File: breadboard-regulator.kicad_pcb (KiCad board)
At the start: 2 copper layers, 16 parts, among them J1 Barrel_Jack_Switch, U1 LM7805_TO220, U2 LD1117S33TR_SOT223

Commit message: finish schematic and PCB design
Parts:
- added J2: Conn_01x02_Pin, Connector_PinHeader_2.54mm:PinHeader_1x02_P2.54mm_Vertical, F.Cu at (224.7, 87.5)
- added J3: Conn_01x02_Pin, Connector_PinHeader_2.54mm:PinHeader_1x02_P2.54mm_Vertical, F.Cu at (224.3, 121.9)
- U2: value LD1117S33TR_SOT223 -> LD1117V33_TO-220
- moved D2 15.9 mm to (214.1, 90.7), turned to 180 degrees
- moved D3 15.8 mm to (213.7, 126.0), turned to 180 degrees
- moved CNF4 5.46 mm to (183.1, 126.2)
- moved CNF3 4.40 mm to (130.2, 124.5)
- moved CNF2 4.22 mm to (183.1, 90.7)
- moved J1 3.76 mm to (83.1, 113.3)
- moved R1 3.22 mm to (203.1, 90.7)
- moved U1 2.80 mm to (148.4, 90.8)
- moved R2 1.78 mm to (204.6, 126.2)
- moved C2 1.03 mm to (171.0, 90.8)
- moved C1 0.41 mm to (113.7, 90.6)
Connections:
- D2 pad 1: unconnected-(D2-K-Pad1) -> GND
- D3 pad 1: unconnected-(D3-K-Pad1) -> GND
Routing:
- net GND: track 0.00 -> 391.8 mm
- net Net-(D1-K): track 0.00 -> 137.1 mm
- net +3.3V: track 0.00 -> 92.9 mm
- net +5V: track 0.00 -> 76.6 mm
- net Net-(D2-A): track 0.00 -> 8.52 mm
- net Net-(D1-A): track 0.00 -> 6.89 mm
- net Net-(D3-A): track 0.00 -> 6.66 mm
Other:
- board outline added: 166.1 x 51.2 mm
- board text added: "+3.3V"
- board text added: "+5V"
- board text added: "GND"
- board text added: "VCC"

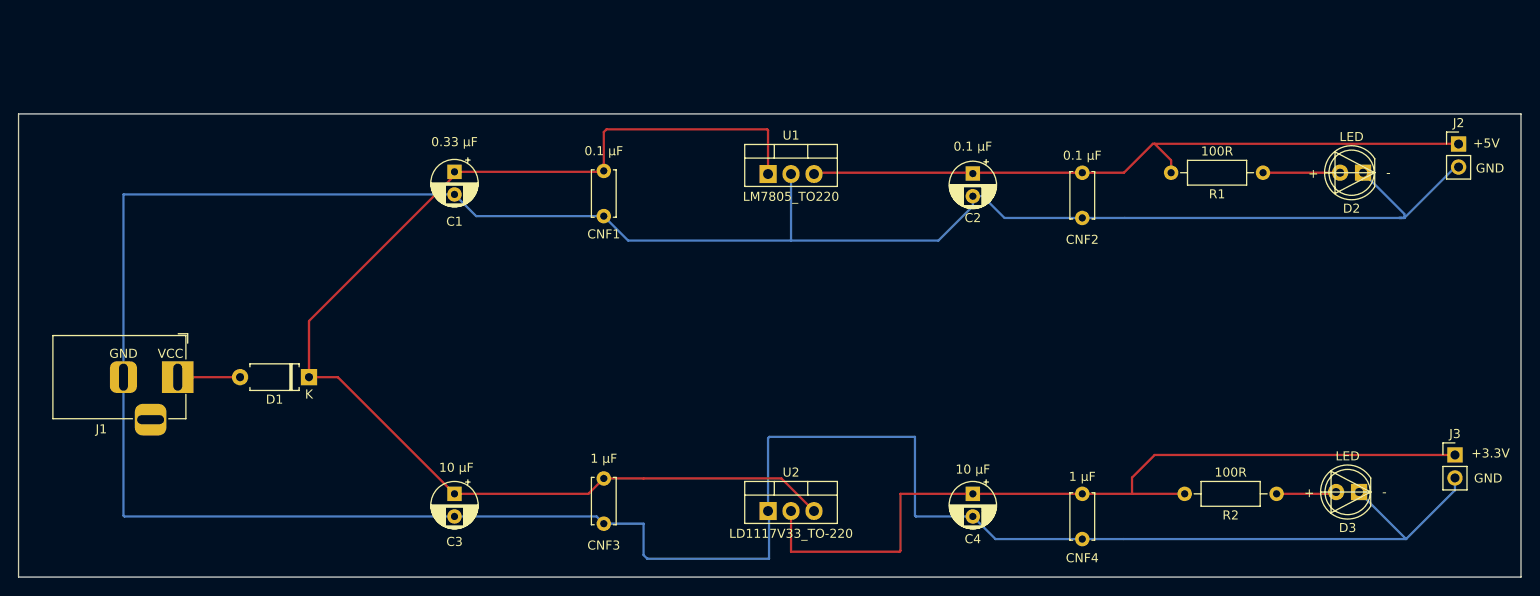
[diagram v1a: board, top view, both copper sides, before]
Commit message: split schematics diagram; rearrange PCB
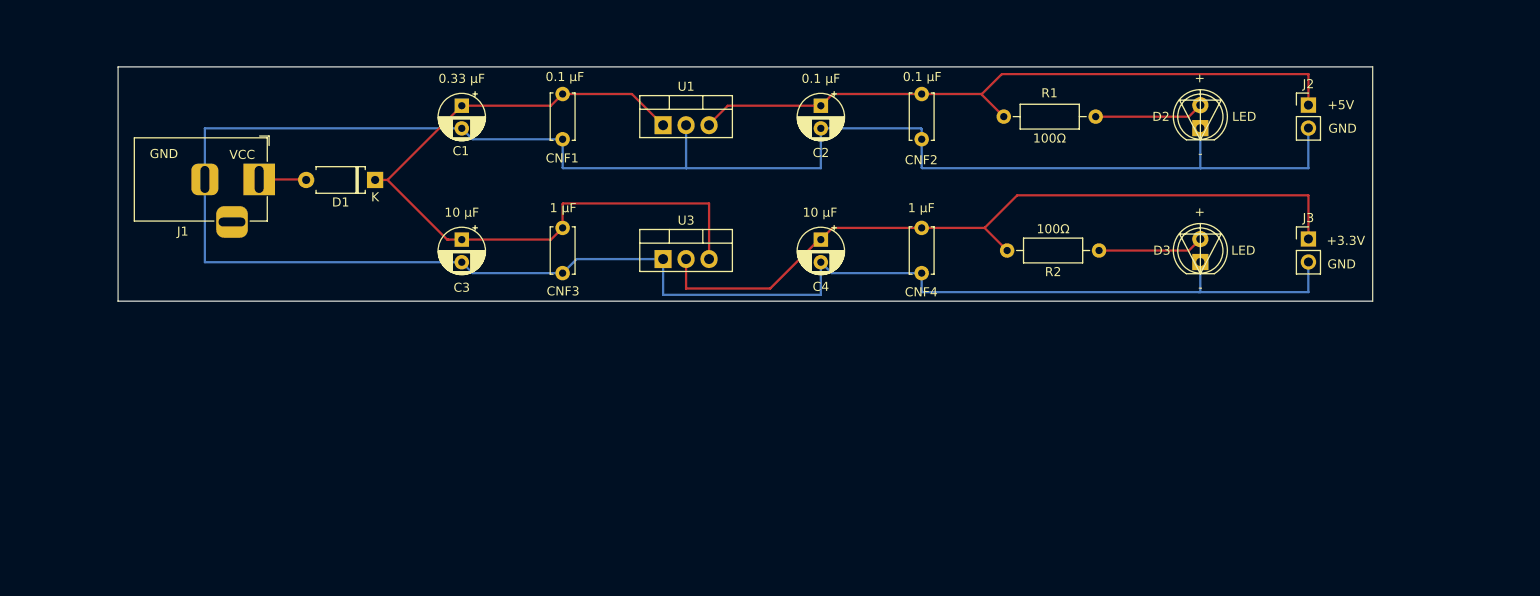
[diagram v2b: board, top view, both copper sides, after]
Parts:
- removed U2: LD1117V33_TO-220, Package_TO_SOT_THT:TO-220-3_Vertical
- added U3: LD1117V33_TO-220, Package_TO_SOT_THT:TO-220-3_Vertical, F.Cu at (136.8, 100.2)
- R1, R2: value 100R -> 100Ω
- moved CNF4 34.3 mm to (165.3, 96.8)
- moved R2 33.3 mm to (185.0, 99.3)
- moved C4 32.7 mm to (154.2, 98.1)
- moved D3 30.9 mm to (196.2, 100.6), turned to 90 degrees
- moved J3 28.9 mm to (208.1, 98.0)
- moved C3 28.1 mm to (114.5, 98.1)
- moved CNF3 28.1 mm to (125.6, 96.8)
- moved J1 23.6 mm to (92.1, 91.4)
- moved D1 23.0 mm to (104.9, 91.5)
- moved CNF2 19.8 mm to (165.3, 82.0)
- moved R1 19.5 mm to (184.6, 84.5)
- moved D2 18.7 mm to (196.2, 85.8), turned to 90 degrees
- moved C2 18.4 mm to (154.2, 83.3)
- moved J2 17.1 mm to (208.1, 83.2)
- moved U1 12.8 mm to (136.8, 85.4)
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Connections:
- net Net-(D1-K) renamed +12V
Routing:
- net GND: track 391.8 -> 302.9 mm
- net +12V: track 137.1 -> 84.8 mm
- net +3.3V: track 92.9 -> 84.7 mm
- net Net-(D3-A): track 6.66 -> 11.7 mm
- net Net-(D2-A): track 8.52 -> 12.1 mm
- net Net-(D1-A): track 6.89 -> 5.22 mm
- net +5V: track 76.6 -> 75.6 mm
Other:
- board size 166.1 x 51.2 mm -> 138.7 x 25.9 mm

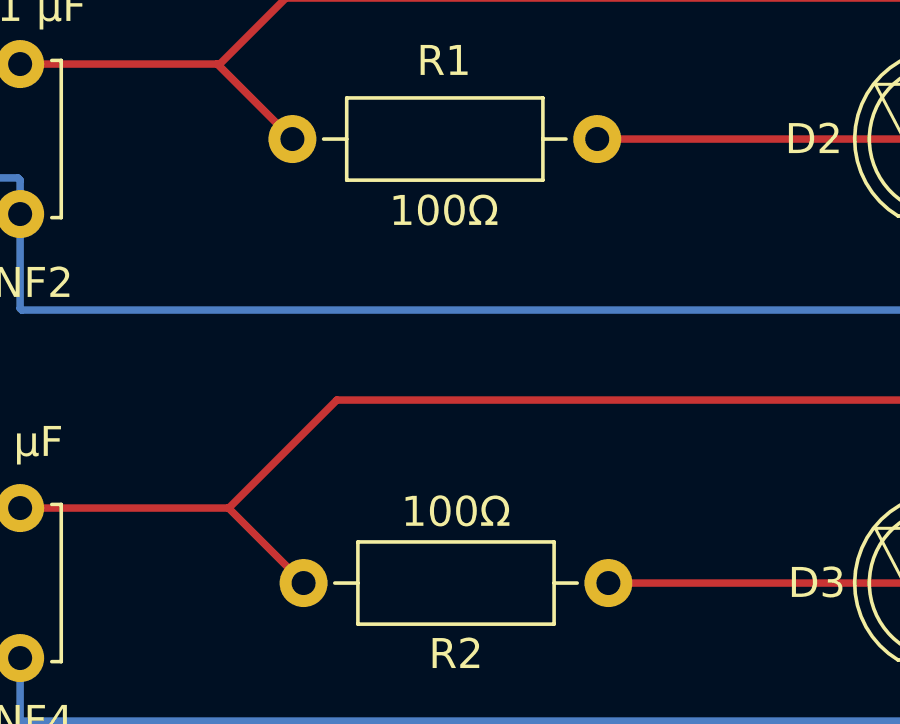
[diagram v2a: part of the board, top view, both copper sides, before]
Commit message: modify net number
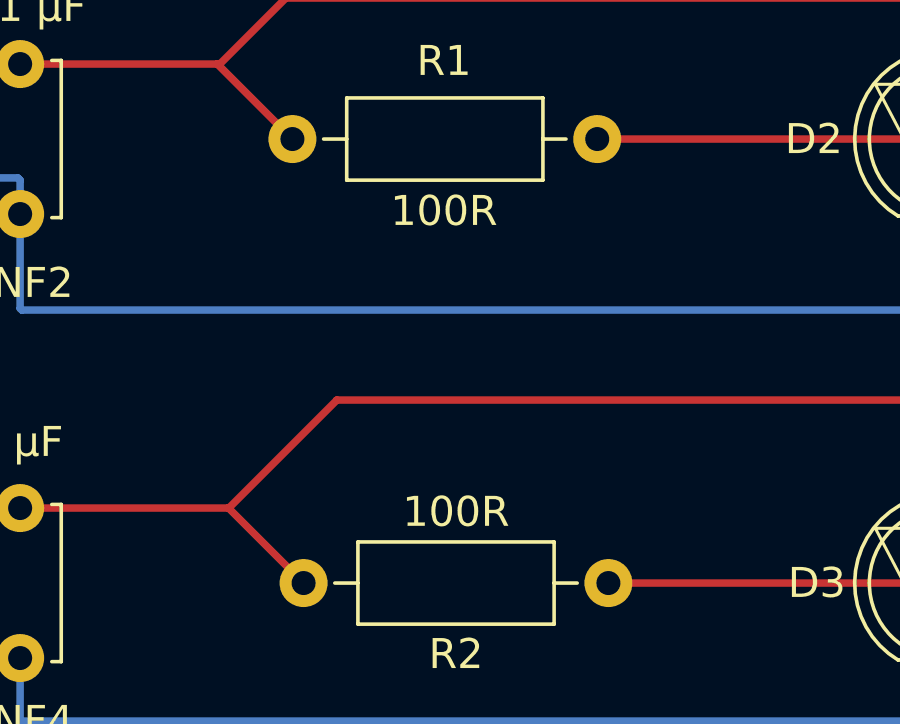
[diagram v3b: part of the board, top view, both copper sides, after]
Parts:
- R1, R2: value 100Ω -> 100R
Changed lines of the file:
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@@
   (net 3 "+5V")
   (net 4 "+3.3V")
-  (net 5 "Net-(D1-A)")
-  (net 6 "Net-(D2-A)")
-  (net 7 "Net-(D3-A)")
-  (net 8 "unconnected-(J1-Pad3)")
+  (net 5 "Net-(D2-A)")
+  (net 6 "Net-(D3-A)")
+  (net 7 "unconnected-(J1-Pad3)")
+  (net 8 "Net-(D1-A)")
   (footprint "Connector_BarrelJack:BarrelJack_Horizontal" (layer "F.Cu")
     (at 92.1 91.4425)
@@
       (stroke (width 0.1) (type solid)) (layer "F.Fab"))
     (pad "1" thru_hole rect (at 0 0) (size 3.5 3.5) (drill oval 1 3) (layers "*.Cu" "*.Mask")
-      (net 5 "Net-(D1-A)") (pintype "passive"))
+      (net 8 "Net-(D1-A)") (pintype "passive"))
     (pad "2" thru_hole roundrect (at -6 0) (size 3 3.5) (drill oval 1 3) (layers "*.Cu" "*.Mask") (roundrect_rratio 0.25)
       (net 2 "GND") (pintype "passive"))
     (pad "3" thru_hole roundrect (at -3 4.7) (size 3.5 3.5) (drill oval 3 1) (layers "*.Cu" "*.Mask") (roundrect_rratio 0.25)
-      (net 8 "unconnected-(J1-Pad3)") (pintype "passive+no_connect"))
+      (net 7 "unconnected-(J1-Pad3)") (pintype "passive+no_connect"))
     (model "${KICAD6_3DMODEL_DIR}/Connector_BarrelJack.3dshapes/BarrelJack_Horizontal.wrl"
       (offset (xyz 0 0 0))
@@
         (effects (font (size 1 1) (thickness 0.15)))
     )
-    (fp_text value "100Ω" (at 5.08 2.37) (layer "F.SilkS")
+    (fp_text value "100R" (at 5.08 2.37) (layer "F.SilkS")
         (effects (font (size 1 1) (thickness 0.15)))
     )
@@
       (stroke (width 0.1) (type solid)) (layer "F.Fab"))
     (pad "1" thru_hole circle (at 0 0 180) (size 1.6 1.6) (drill 0.8) (layers "*.Cu" "*.Mask")
-      (net 7 "Net-(D3-A)") (pintype "passive"))
+      (net 6 "Net-(D3-A)") (pintype "passive"))
     (pad "2" thru_hole oval (at 10.16 0 180) (size 1.6 1.6) (drill 0.8) (layers "*.Cu" "*.Mask")
       (net 4 "+3.3V") (pintype "passive"))
@@
       (net 2 "GND") (pinfunction "K") (pintype "passive"))
     (pad "2" thru_hole circle (at 2.54 0 90) (size 1.8 1.8) (drill 0.9) (layers "*.Cu" "*.Mask")
-      (net 6 "Net-(D2-A)") (pinfunction "A") (pintype "passive"))
+      (net 5 "Net-(D2-A)") (pinfunction "A") (pintype "passive"))
     (model "${KICAD6_3DMODEL_DIR}/LED_THT.3dshapes/LED_D5.0mm.wrl"
       (offset (xyz 0 0 0))
@@
       (net 1 "+12V") (pinfunction "K") (pintype "passive"))
     (pad "2" thru_hole oval (at 7.62 0 180) (size 1.8 1.8) (drill 0.9) (layers "*.Cu" "*.Mask")
-      (net 5 "Net-(D1-A)") (pinfunction "A") (pintype "passive"))
+      (net 8 "Net-(D1-A)") (pinfunction "A") (pintype "passive"))
     (model "${KICAD6_3DMODEL_DIR}/Diode_THT.3dshapes/D_A-405_P7.62mm_Horizontal.wrl"
       (offset (xyz 0 0 0))
@@
       (net 2 "GND") (pinfunction "K") (pintype "passive"))
     (pad "2" thru_hole circle (at 2.54 0 90) (size 1.8 1.8) (drill 0.9) (layers "*.Cu" "*.Mask")
-      (net 7 "Net-(D3-A)") (pinfunction "A") (pintype "passive"))
+      (net 6 "Net-(D3-A)") (pinfunction "A") (pintype "passive"))
     (model "${KICAD6_3DMODEL_DIR}/LED_THT.3dshapes/LED_D5.0mm.wrl"
       (offset (xyz 0 0 0))
@@
         (effects (font (size 1 1) (thickness 0.15)))
     )
-    (fp_text value "100Ω" (at 5.107145 -2.4) (layer "F.SilkS")
+    (fp_text value "100R" (at 5.107145 -2.4) (layer "F.SilkS")
         (effects (font (size 1 1) (thickness 0.15)))
     )
@@
       (stroke (width 0.1) (type solid)) (layer "F.Fab"))
     (pad "1" thru_hole circle (at 0 0 180) (size 1.6 1.6) (drill 0.8) (layers "*.Cu" "*.Mask")
-      (net 6 "Net-(D2-A)") (pintype "passive"))
+      (net 5 "Net-(D2-A)") (pintype "passive"))
     (pad "2" thru_hole oval (at 10.16 0 180) (size 1.6 1.6) (drill 0.8) (layers "*.Cu" "*.Mask")
       (net 3 "+5V") (pintype "passive"))
@@
   (segment (start 172.292855 96.8) (end 174.792855 99.3) (width 0.25) (layer "F.Cu") (net 4))
   (segment (start 154.005112 98.094888) (end 154.195713 98.094888) (width 0.25) (layer "F.Cu") (net 4))
-  (segment (start 97.2425 91.4425) (end 97.3 91.5) (width 0.25) (layer "F.Cu") (net 5))
-  (segment (start 92.1 91.4425) (end 97.2425 91.4425) (width 0.25) (layer "F.Cu") (net 5))
-  (segment (start 184.58 84.5) (end 194.886426 84.5) (width 0.25) (layer "F.Cu") (net 6))
-  (segment (start 194.886426 84.5) (end 196.151426 83.235) (width 0.25) (layer "F.Cu") (net 6))
-  (segment (start 184.952855 99.3) (end 194.886426 99.3) (width 0.25) (layer "F.Cu") (net 7))
-  (segment (start 194.886426 99.3) (end 196.151426 98.035) (width 0.25) (layer "F.Cu") (net 7))
+  (segment (start 184.58 84.5) (end 194.886426 84.5) (width 0.25) (layer "F.Cu") (net 5))
+  (segment (start 194.886426 84.5) (end 196.151426 83.235) (width 0.25) (layer "F.Cu") (net 5))
+  (segment (start 184.952855 99.3) (end 194.886426 99.3) (width 0.25) (layer "F.Cu") (net 6))
+  (segment (start 194.886426 99.3) (end 196.151426 98.035) (width 0.25) (layer "F.Cu") (net 6))
+  (segment (start 97.2425 91.4425) (end 97.3 91.5) (width 0.25) (layer "F.Cu") (net 8))
+  (segment (start 92.1 91.4425) (end 97.2425 91.4425) (width 0.25) (layer "F.Cu") (net 8))
 )

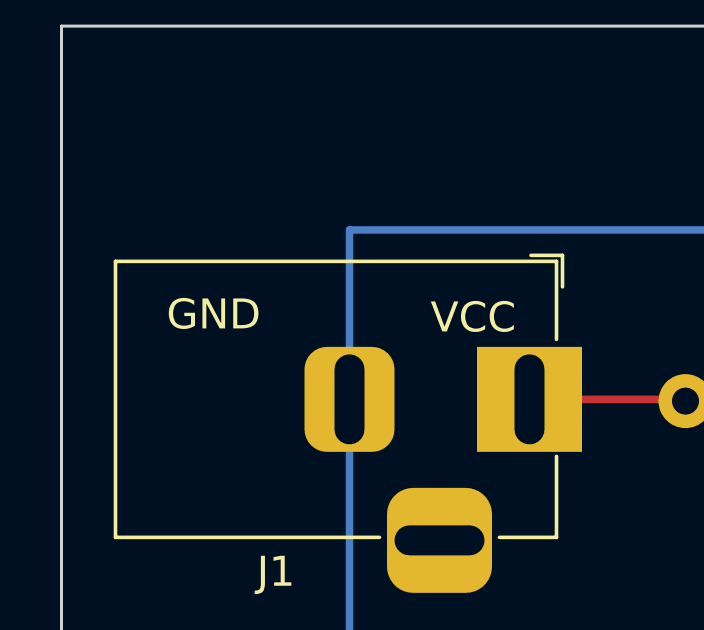
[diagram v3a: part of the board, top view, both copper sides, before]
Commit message: change from GND to GNDREF
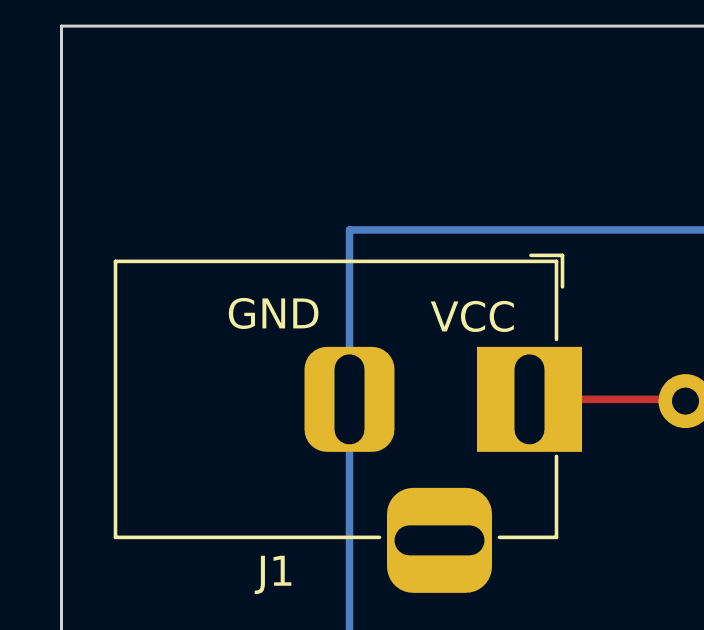
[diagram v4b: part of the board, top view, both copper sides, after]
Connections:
- net GND renamed GNDREF
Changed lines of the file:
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@@
   (net 0 "")
   (net 1 "+12V")
-  (net 2 "GND")
+  (net 2 "GNDREF")
   (net 3 "+5V")
   (net 4 "+3.3V")
@@
       (net 8 "Net-(D1-A)") (pintype "passive"))
     (pad "2" thru_hole roundrect (at -6 0) (size 3 3.5) (drill oval 1 3) (layers "*.Cu" "*.Mask") (roundrect_rratio 0.25)
-      (net 2 "GND") (pintype "passive"))
+      (net 2 "GNDREF") (pintype "passive"))
     (pad "3" thru_hole roundrect (at -3 4.7) (size 3.5 3.5) (drill oval 3 1) (layers "*.Cu" "*.Mask") (roundrect_rratio 0.25)
       (net 7 "unconnected-(J1-Pad3)") (pintype "passive+no_connect"))
@@
       (net 3 "+5V") (pinfunction "Pin_1") (pintype "passive"))
     (pad "2" thru_hole oval (at 0 2.54) (size 1.7 1.7) (drill 1) (layers "*.Cu" "*.Mask")
-      (net 2 "GND") (pinfunction "Pin_2") (pintype "passive"))
+      (net 2 "GNDREF") (pinfunction "Pin_2") (pintype "passive"))
     (model "${KICAD6_3DMODEL_DIR}/Connector_PinHeader_2.54mm.3dshapes/PinHeader_1x02_P2.54mm_Vertical.wrl"
       (offset (xyz 0 0 0))
@@
       (net 1 "+12V") (pinfunction "VI") (pintype "power_in"))
     (pad "2" thru_hole oval (at 2.54 0) (size 1.905 2) (drill 1.1) (layers "*.Cu" "*.Mask")
-      (net 2 "GND") (pinfunction "GND") (pintype "power_in"))
+      (net 2 "GNDREF") (pinfunction "GND") (pintype "power_in"))
     (pad "3" thru_hole oval (at 5.08 0) (size 1.905 2) (drill 1.1) (layers "*.Cu" "*.Mask")
       (net 3 "+5V") (pinfunction "VO") (pintype "power_out"))
@@
       (net 1 "+12V") (pintype "passive"))
     (pad "2" thru_hole circle (at 2.5 0 270) (size 1.6 1.6) (drill 0.8) (layers "*.Cu" "*.Mask")
-      (net 2 "GND") (pintype "passive"))
+      (net 2 "GNDREF") (pintype "passive"))
     (model "${KICAD6_3DMODEL_DIR}/Capacitor_THT.3dshapes/CP_Radial_D5.0mm_P2.50mm.wrl"
       (offset (xyz 0 0 0))
@@
       (stroke (width 0.1) (type solid)) (layer "F.Fab"))
     (pad "1" thru_hole rect (at 0 0) (size 1.905 2) (drill 1.1) (layers "*.Cu" "*.Mask")
-      (net 2 "GND") (pinfunction "GND") (pintype "power_in"))
+      (net 2 "GNDREF") (pinfunction "GND") (pintype "power_in"))
     (pad "2" thru_hole oval (at 2.54 0) (size 1.905 2) (drill 1.1) (layers "*.Cu" "*.Mask")
       (net 4 "+3.3V") (pinfunction "VO") (pintype "power_out"))
@@
       (net 4 "+3.3V") (pintype "passive"))
     (pad "2" thru_hole circle (at 5 0 270) (size 1.6 1.6) (drill 0.8) (layers "*.Cu" "*.Mask")
-      (net 2 "GND") (pintype "passive"))
+      (net 2 "GNDREF") (pintype "passive"))
     (model "${KICAD6_3DMODEL_DIR}/Capacitor_THT.3dshapes/C_Disc_D5.0mm_W2.5mm_P5.00mm.wrl"
       (offset (xyz 0 0 0))
@@
       (net 4 "+3.3V") (pintype "passive"))
     (pad "2" thru_hole circle (at 2.5 0 270) (size 1.6 1.6) (drill 0.8) (layers "*.Cu" "*.Mask")
-      (net 2 "GND") (pintype "passive"))
+      (net 2 "GNDREF") (pintype "passive"))
     (model "${KICAD6_3DMODEL_DIR}/Capacitor_THT.3dshapes/CP_Radial_D5.0mm_P2.50mm.wrl"
       (offset (xyz 0 0 0))
@@
       (net 4 "+3.3V") (pinfunction "Pin_1") (pintype "passive"))
     (pad "2" thru_hole oval (at 0 2.54) (size 1.7 1.7) (drill 1) (layers "*.Cu" "*.Mask")
-      (net 2 "GND") (pinfunction "Pin_2") (pintype "passive"))
+      (net 2 "GNDREF") (pinfunction "Pin_2") (pintype "passive"))
     (model "${KICAD6_3DMODEL_DIR}/Connector_PinHeader_2.54mm.3dshapes/PinHeader_1x02_P2.54mm_Vertical.wrl"
       (offset (xyz 0 0 0))
@@
       (net 1 "+12V") (pintype "passive"))
     (pad "2" thru_hole circle (at 5 0 270) (size 1.6 1.6) (drill 0.8) (layers "*.Cu" "*.Mask")
-      (net 2 "GND") (pintype "passive"))
+      (net 2 "GNDREF") (pintype "passive"))
     (model "${KICAD6_3DMODEL_DIR}/Capacitor_THT.3dshapes/C_Disc_D5.0mm_W2.5mm_P5.00mm.wrl"
       (offset (xyz 0 0 0))
@@
       (stroke (width 0.1) (type solid)) (fill none) (layer "F.Fab"))
     (pad "1" thru_hole rect (at 0 0 90) (size 1.8 1.8) (drill 0.9) (layers "*.Cu" "*.Mask")
-      (net 2 "GND") (pinfunction "K") (pintype "passive"))
+      (net 2 "GNDREF") (pinfunction "K") (pintype "passive"))
     (pad "2" thru_hole circle (at 2.54 0 90) (size 1.8 1.8) (drill 0.9) (layers "*.Cu" "*.Mask")
       (net 5 "Net-(D2-A)") (pinfunction "A") (pintype "passive"))
@@
       (net 1 "+12V") (pintype "passive"))
     (pad "2" thru_hole circle (at 5 0 270) (size 1.6 1.6) (drill 0.8) (layers "*.Cu" "*.Mask")
-      (net 2 "GND") (pintype "passive"))
+      (net 2 "GNDREF") (pintype "passive"))
     (model "${KICAD6_3DMODEL_DIR}/Capacitor_THT.3dshapes/C_Disc_D5.0mm_W2.5mm_P5.00mm.wrl"
       (offset (xyz 0 0 0))
@@
       (net 3 "+5V") (pintype "passive"))
     (pad "2" thru_hole circle (at 2.5 0 270) (size 1.6 1.6) (drill 0.8) (layers "*.Cu" "*.Mask")
-      (net 2 "GND") (pintype "passive"))
+      (net 2 "GNDREF") (pintype "passive"))
     (model "${KICAD6_3DMODEL_DIR}/Capacitor_THT.3dshapes/CP_Radial_D5.0mm_P2.50mm.wrl"
       (offset (xyz 0 0 0))
@@
       (net 1 "+12V") (pintype "passive"))
     (pad "2" thru_hole circle (at 2.5 0 270) (size 1.6 1.6) (drill 0.8) (layers "*.Cu" "*.Mask")
-      (net 2 "GND") (pintype "passive"))
+      (net 2 "GNDREF") (pintype "passive"))
     (model "${KICAD6_3DMODEL_DIR}/Capacitor_THT.3dshapes/CP_Radial_D5.0mm_P2.50mm.wrl"
       (offset (xyz 0 0 0))
@@
       (net 3 "+5V") (pintype "passive"))
     (pad "2" thru_hole circle (at 5 0 270) (size 1.6 1.6) (drill 0.8) (layers "*.Cu" "*.Mask")
-      (net 2 "GND") (pintype "passive"))
+      (net 2 "GNDREF") (pintype "passive"))
     (model "${KICAD6_3DMODEL_DIR}/Capacitor_THT.3dshapes/C_Disc_D5.0mm_W2.5mm_P5.00mm.wrl"
       (offset (xyz 0 0 0))
@@
       (stroke (width 0.1) (type solid)) (fill none) (layer "F.Fab"))
     (pad "1" thru_hole rect (at 0 0 90) (size 1.8 1.8) (drill 0.9) (layers "*.Cu" "*.Mask")
-      (net 2 "GND") (pinfunction "K") (pintype "passive"))
+      (net 2 "GNDREF") (pinfunction "K") (pintype "passive"))
     (pad "2" thru_hole circle (at 2.54 0 90) (size 1.8 1.8) (drill 0.9) (layers "*.Cu" "*.Mask")
       (net 6 "Net-(D3-A)") (pinfunction "A") (pintype "passive"))
@@
     (effects (font (size 1 1) (thickness 0.15)) (justify left bottom))
   )
-  (gr_text "GND" (at 80 89.2) (layer "F.SilkS")
+  (gr_text "GND" (at 82 89.2) (layer "F.SilkS")
     (effects (font (size 1 1) (thickness 0.15)) (justify left bottom))
   )
